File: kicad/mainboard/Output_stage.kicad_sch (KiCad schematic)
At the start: 41 parts, among them J6 OUTPUT A, J7 OUTPUT B, T1 IRL520N, T2 IRL520N, T3 IRF9Z24, T4 IRL520N, T5 IRL520N, T6 IRF9Z24, U10 LM358N, U8 LTC1661

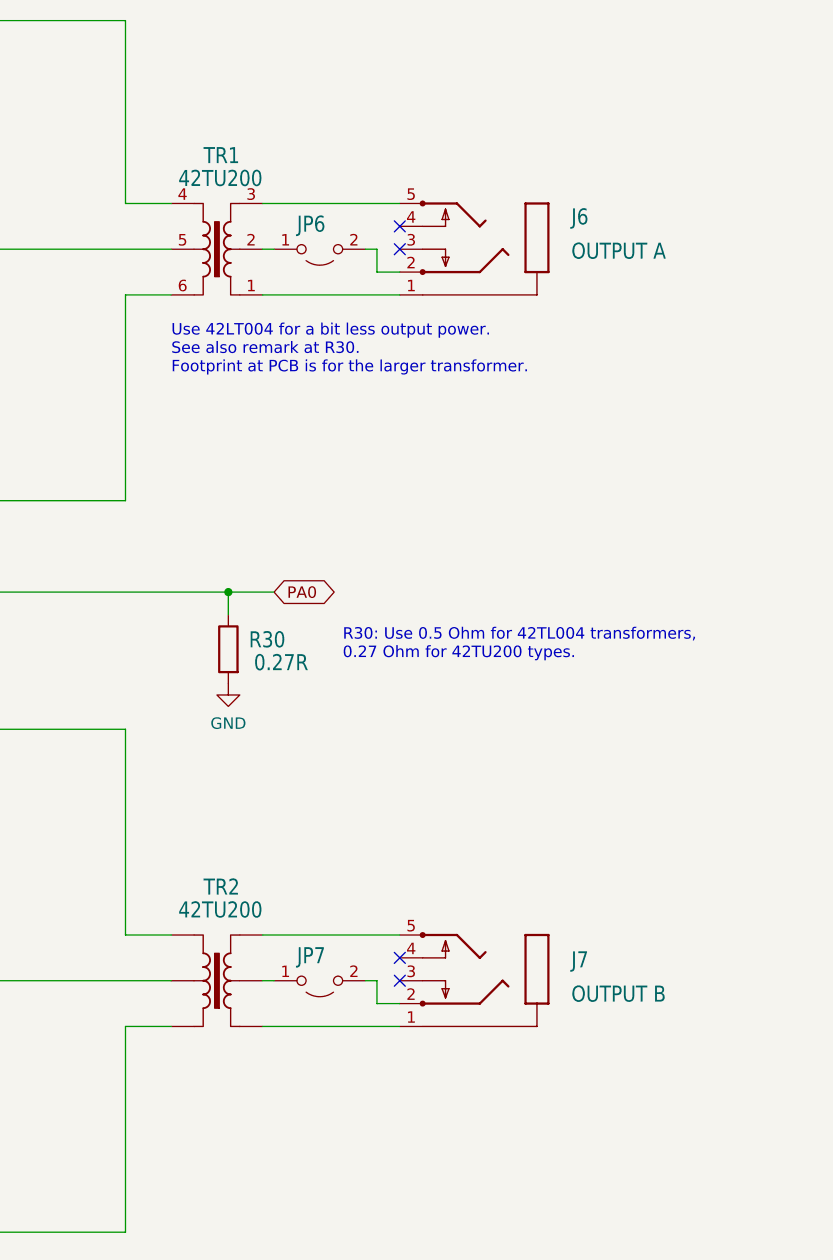
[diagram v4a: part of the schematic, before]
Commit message: Fixed footprint for powerbus connector. Bumped version to 1.4.1.
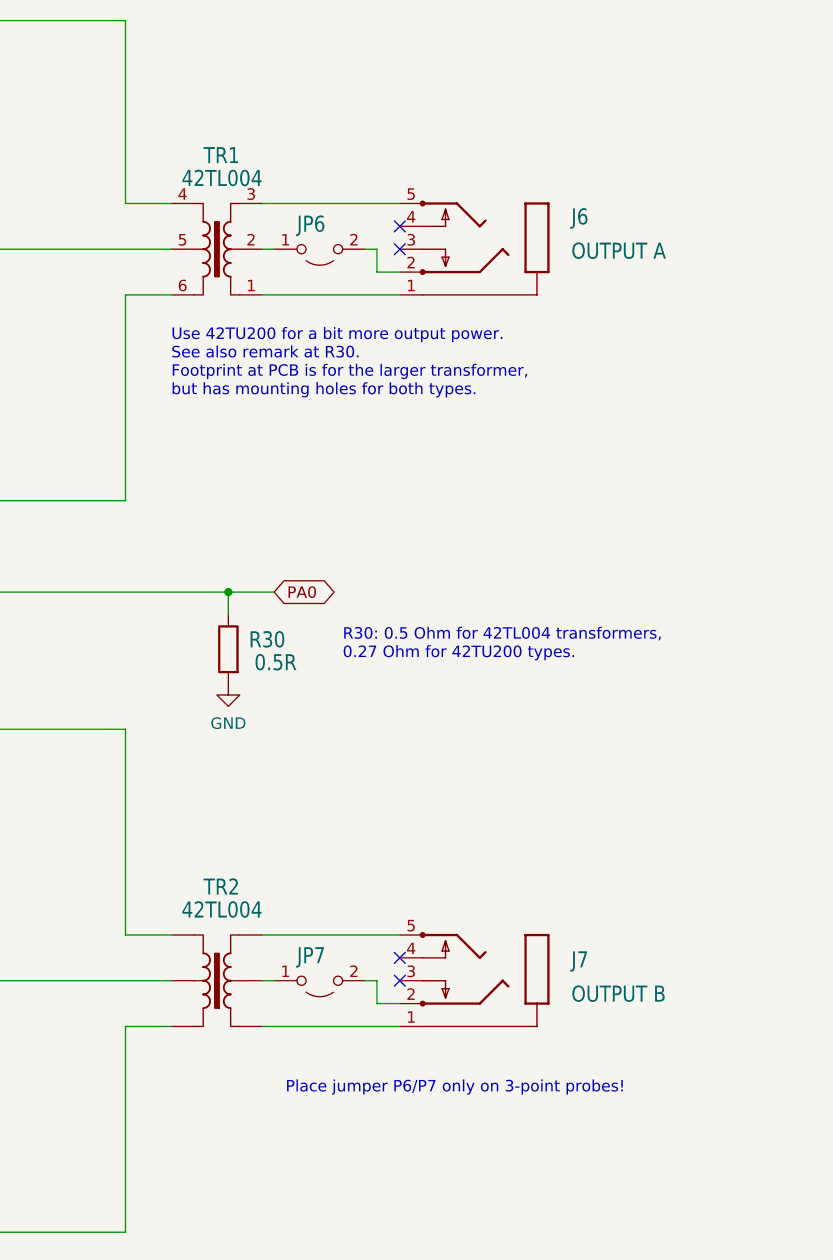
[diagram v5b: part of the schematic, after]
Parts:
- R30: value 0.27R -> 0.5R
- TR1, TR2: value 42TU200 -> 42TL004
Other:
- note added: "Place jumper P6/P7 only on 3-point probes!"
- note added: "R30: 0.5 Ohm for 42TL004 transformers, 0.27 Ohm for 42TU200 types."
- note added: "Use 42TU200 for a bit more output power. See also remark at R30. Footprint at PCB is for the larger transformer, but has mounting holes for both types."
- note removed: "R30: Use 0.5 Ohm for 42TL004 transformers, 0.27 Ohm for 42TU200 types."
- note removed: "Use 42LT004 for a bit less output power. See also remark at R30. Footprint at PCB is for the larger transformer."
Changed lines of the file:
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@@
   (title_block
     (title "Output stage")
-    (date "2022-08-01")
-    (rev "1.3-Chi")
+    (date "2022-09-04")
+    (rev "1.4.1-chi")
   )
   (junction (at 154.94 158.75) (diameter 0) (color 0 0 0 0)
@@
     (effects (font (size 1.27 1.27)) (justify right bottom))
   )
-  (text "R30: Use 0.5 Ohm for 42TL004 transformers, \n0.27 Ohm for 42TU200 types."
+  (text "R30: 0.5 Ohm for 42TL004 transformers, \n0.27 Ohm for 42TU200 types."
     (at 229.87 90.17 0)
     (effects (font (size 1.27 1.27)) (justify left bottom))
   )
-  (text "Use 42LT004 for a bit less output power. \nSee also remark at R30.\nFootprint at PCB is for the larger transformer."
-    (at 210.82 58.42 0)
+  (text "Use 42TU200 for a bit more output power. \nSee also remark at R30.\nFootprint at PCB is for the larger transformer,\nbut has mounting holes for both types."
+    (at 210.82 60.96 0)
+    (effects (font (size 1.27 1.27)) (justify left bottom))
+  )
+  (text "Place jumper P6/P7 only on 3-point probes!" (at 223.52 138.43 0)
     (effects (font (size 1.27 1.27)) (justify left bottom))
   )
@@
       (effects (font (size 1.778 1.5113)) (justify left bottom))
     )
-    (property "Value" "42TU200" (id 1) (at 220.98 35.56 0)
+    (property "Value" "42TL004" (id 1) (at 220.98 35.56 0)
       (effects (font (size 1.778 1.5113)) (justify left bottom))
     )
@@
       (effects (font (size 1.778 1.5113)) (justify left bottom))
     )
-    (property "Value" "0.27R" (id 1) (at 226.06 91.44 0)
+    (property "Value" "0.5R" (id 1) (at 224.79 91.44 0)
       (effects (font (size 1.778 1.5113)) (justify left bottom))
     )
@@
       (effects (font (size 1.778 1.5113)) (justify left bottom))
     )
-    (property "Value" "42TU200" (id 1) (at 220.98 116.84 0)
-      (effects (font (size 1.778 1.5113)) (justify left bottom))
-    )
+    (property "Value" "42TL004" (id 1) (at 220.98 116.84 0)
+      (effects (font (size 1.778 1.5113)) (justify left bottom))
+    )
